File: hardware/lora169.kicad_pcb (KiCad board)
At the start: 2 copper layers, 60 x 50 mm, 4 parts, among them U1 XIAO-ESP32-S3-DIP, U2 E22-170M30S-SX1262

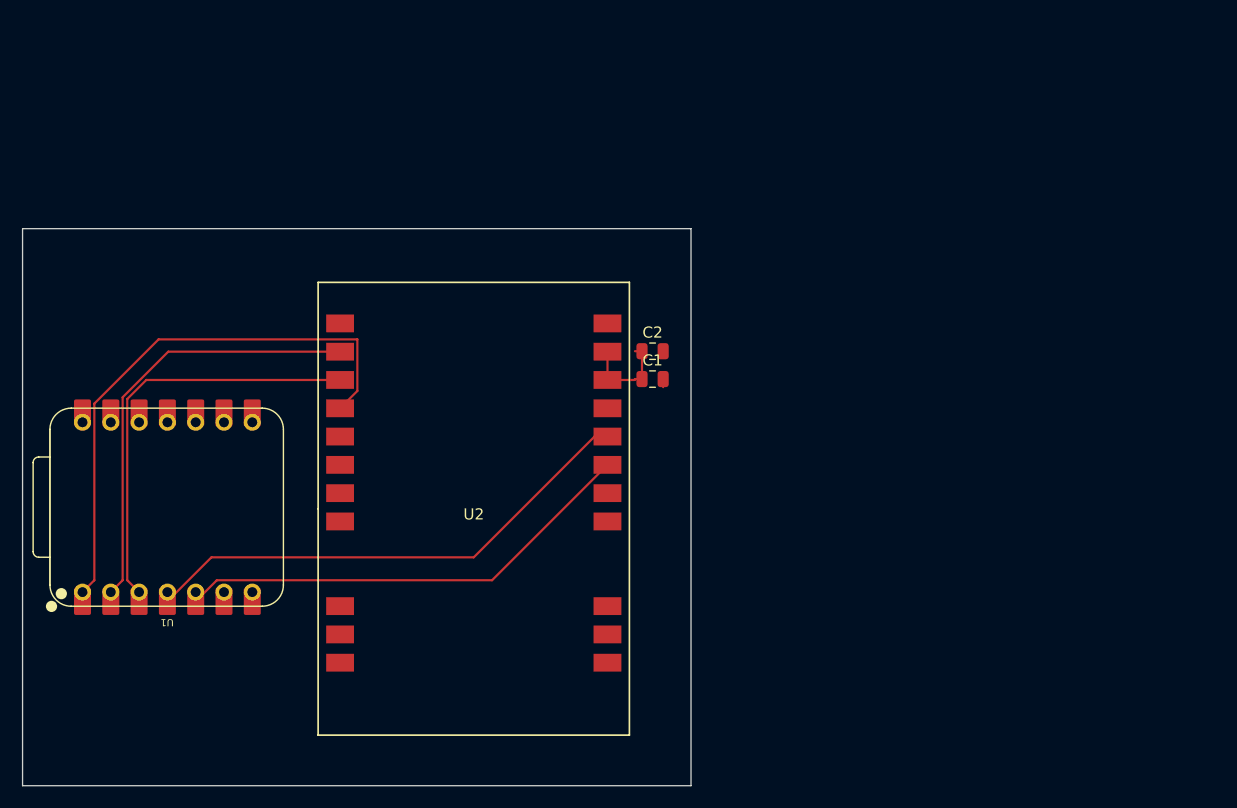
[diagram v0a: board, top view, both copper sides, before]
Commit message: Refonte from scratch carte mère adaptée au breakout E22 + finitions
Carte mère reconçue pour recevoir le breakout E22 plutôt que le module
soudé direct. Trois composants seulement : XIAO ESP32-S3 DIP, plus
deux embases femelles 1×11 (PinSocket_2.54mm) espacées de 32,1 mm
centre à centre pour matcher les pin headers du breakout.

Schéma : labels signaux (NRST, DIO1, BUSY, TXEN, RXEN, NSS, SCK, MISO,
MOSI), power ports +5V (au lieu de +3V3) sur la pin VBUS du XIAO et
les broches VCC du connecteur — alimentation passe maintenant par
VBUS pour permettre la pleine puissance 30 dBm hardware. NC flags sur
DIO2, ANT, et pins XIAO réserve.

PCB compact 80 × 55 mm avec contour Edge.Cuts, USB-C du XIAO en bord
gauche pour découpe boîtier simple. Routage manuel en F.Cu pour
préserver la continuité du plan de masse face arrière, avec inversions
MISO↔MOSI et NRST↔DIO1 dans le firmware pour éliminer les croisements
géométriques. Zones GND coulées sur F.Cu et B.Cu en mode pleine
connexion.

DRC : 0 erreur, 0 pad non connecté. Les warnings restants sont
purement cosmétiques (silkscreen XIAO qui dépasse du bord PCB côté
USB-C — attendu).

Breakout E22 : ajustements mineurs après finalisation du DRC.

.gitignore élargi : **/fab/ pour ignorer les Gerbers de tous les
sous-projets, *-gerbers.zip pour les ZIP d'upload, *.dsn / *.ses pour
les intermédiaires Freerouting.

Co-Authored-By: Claude Opus 4.7 (1M context) <noreply@anthropic.com>
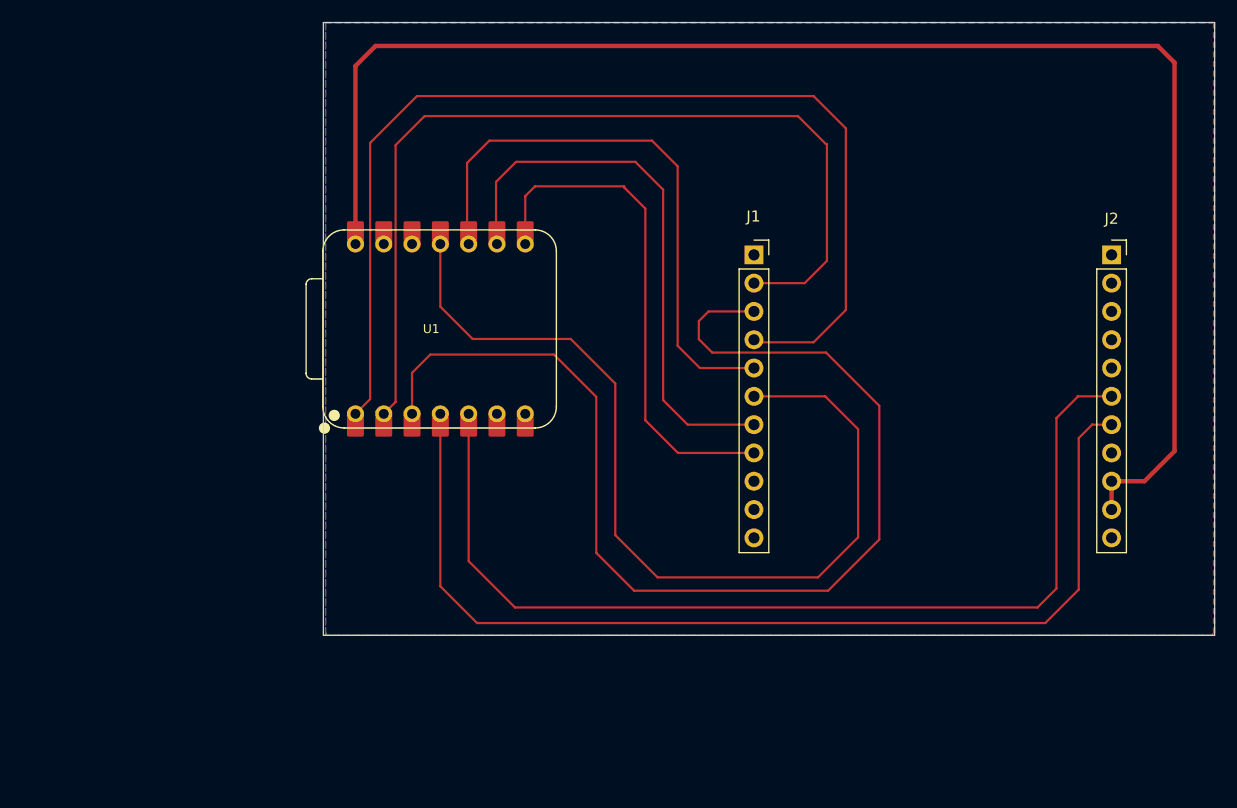
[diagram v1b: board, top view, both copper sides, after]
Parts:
- removed C1: 100nF, Capacitor_SMD:C_0805_2012Metric
- removed C2: 10uF, Capacitor_SMD:C_0805_2012Metric
- removed U2: E22-170M30S-SX1262, Ebyte_E22:E22-170M30S-SX1262
- added J1: Conn_01x11, Connector_PinSocket_2.54mm:PinSocket_1x11_P2.54mm_Vertical, F.Cu at (128.7, 70.8)
- added J2: Conn_01x11, Connector_PinSocket_2.54mm:PinSocket_1x11_P2.54mm_Vertical, F.Cu at (160.8, 70.8)
- moved U1 29.3 mm to (100.5, 77.5)
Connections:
- U1 pad 12: +3V3 -> unconnected-(U1-3V3-Pad12)
- U1 pad 14: unconnected-(U1-VBUS-Pad14) -> +5V
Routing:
- net +5V: track 0.00 -> 135.0 mm
- net /MOSI: track 0.00 -> 84.3 mm
- net /BUSY: track 37.6 -> 102.8 mm
- net /MISO: track 0.00 -> 51.8 mm
- net /SCK: track 0.00 -> 50.3 mm
- net /RXEN: track 42.0 -> 89.5 mm
- net /TXEN: track 45.6 -> 92.4 mm
- net /NSS: track 0.00 -> 46.3 mm
- net /NRST: track 50.2 -> 96.4 mm
- net /DIO1: track 39.1 -> 83.3 mm
- net +3V3: track 8.91 -> 0.00 mm
- added copper zone on B.Cu, net GND
- added copper zone on F.Cu, net GND
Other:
- board size 60 x 50 mm -> 80 x 55 mm

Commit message: Trous M3 + audit final + boîtier OpenSCAD
Carte mère :
- Ajout de 4 trous de fixation MountingHole_3.2mm_M3 aux coins
  (95,55) (165,55) (95,101) (165,101). Le trou bas-droit est
  asymétrique en Y (Y=101 au lieu de 100) pour éviter le
  courtyards_overlap avec J2 broche 11.
- Audit final : contour 80×55 mm confirmé, 99 segments en F.Cu
  largeurs 0,2 mm (signal) et 0,4 mm (alim +5V), 2 zones GND
  (F.Cu + B.Cu) en pleine connexion, 0 via (les pads THT des
  PinSockets servent de via naturels), 11 nets nommés cohérents
  avec le schéma.
- DRC : 0 erreur, 0 pad non connecté, 0 erreur d'empreinte.
  Prête à fabriquer chez JLCPCB / PCBWay.

Boîtier 3D :
- Modélisation OpenSCAD paramétrique dans enclosure/.
- Cuvette monobloc 90×65×27,6 mm + couvercle plat 90×65×2 mm
  avec rebord intérieur d'engagement par friction (sans vis,
  sans clip).
- 4 piliers à 2 étages au fond pour porter et centrer le PCB
  via ses trous M3.
- Découpe USB-C 11×5 mm en bord gauche, alignée XIAO.
- Trou SMA Ø 6,5 mm centré sur la face droite.

Cleanup :
- Suppression de hardware/breakout-e22/upstream-eagle/ (les
  sources Eagle de NanoVHF, devenues inutiles depuis que le
  breakout est entièrement conçu from scratch).
- README breakout réécrit : caractéristiques techniques précises
  (40,6×46,3 mm, espacement 32,1 mm entre J1/J2) et mapping
  complet des pin headers vers les pads E22.
- README projet : tableau de statut pièce par pièce, section
  architecture détaillée, structure du dépôt à jour.
- .gitignore : ajout de .playwright-mcp/ (cache navigateur MCP).

Co-Authored-By: Claude Opus 4.7 (1M context) <noreply@anthropic.com>
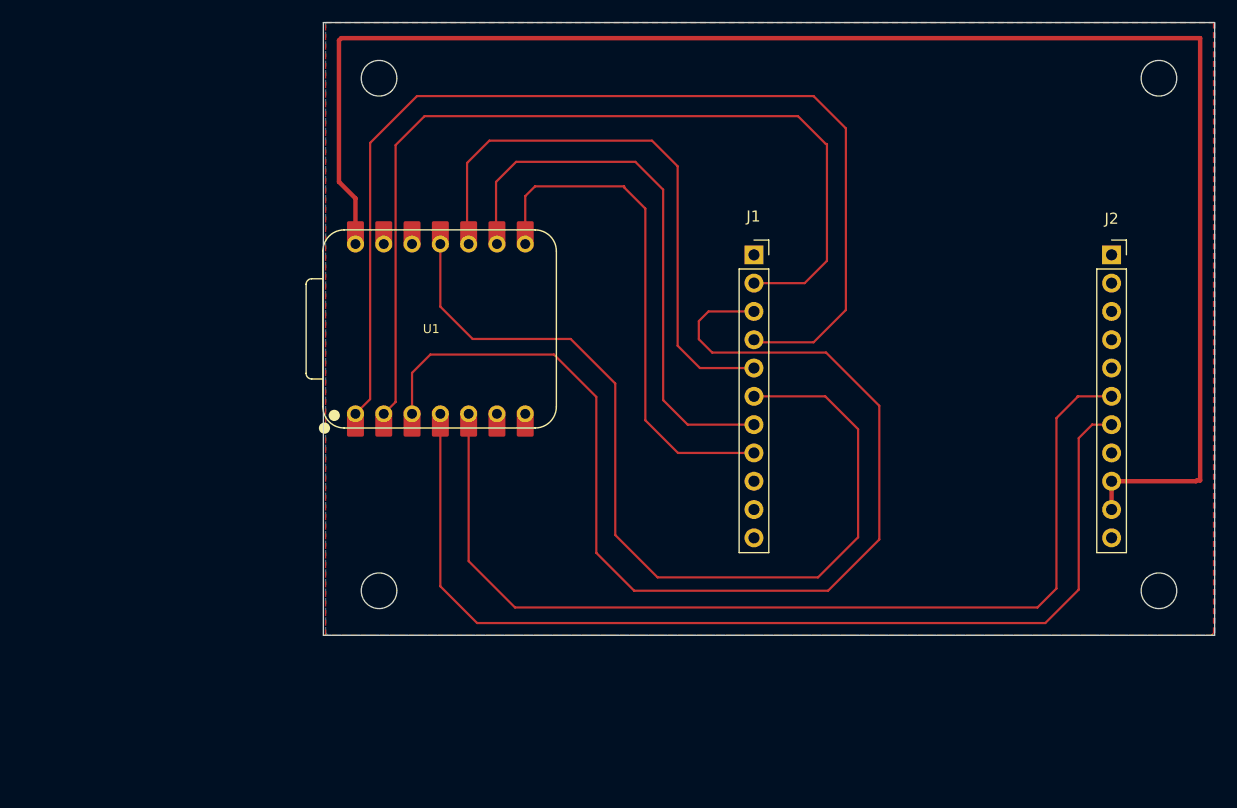
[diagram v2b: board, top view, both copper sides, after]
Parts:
- added REF**: MountingHole_3.2mm_M3, MountingHole:MountingHole_3.2mm_M3, F.Cu at (95.0, 55.0)
- added REF**: MountingHole_3.2mm_M3, MountingHole:MountingHole_3.2mm_M3, F.Cu at (95.0, 101.0)
- added REF**: MountingHole_3.2mm_M3, MountingHole:MountingHole_3.2mm_M3, F.Cu at (165.0, 101.0)
- added REF**: MountingHole_3.2mm_M3, MountingHole:MountingHole_3.2mm_M3, F.Cu at (165.0, 55.0)
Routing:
- net +5V: track 135.0 -> 146.5 mm
